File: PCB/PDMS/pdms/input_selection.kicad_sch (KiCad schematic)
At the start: 31 parts, among them U1 AQY221R4VY, U4 AQY221R4VY, U5 AQY221R4VY, U6 AQY221R4VY

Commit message: Clean-up of schematics
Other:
- note added: "Remember about pull down if safety future is used! R39..R42"
- note added: "Safety section (safety line handler)"
- note added: "TODO Rev 3.0: Add pull-down to all 16-channels input"
- note added: "https://www.mouser.pl/ProductDetail/Panasonic-Industrial-Devices/AQY221R4VY"
- note removed: "PlEASE CLEAN ME UP IF YOU HAVE MORE TIME!!!"
- note removed: "Remember about pull down if safety future is used!"
- note removed: "https://www.mouser.pl/ProductDetail/Panasonic-Industrial-Devices/AQY221R4VY?qs=St27ATL478uV4j9hHKsfjA%3D%3D"
- moved on the sheet: R1, R116, R117, R118, R119, R159, R160, R161, R162, R163, R164, R165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

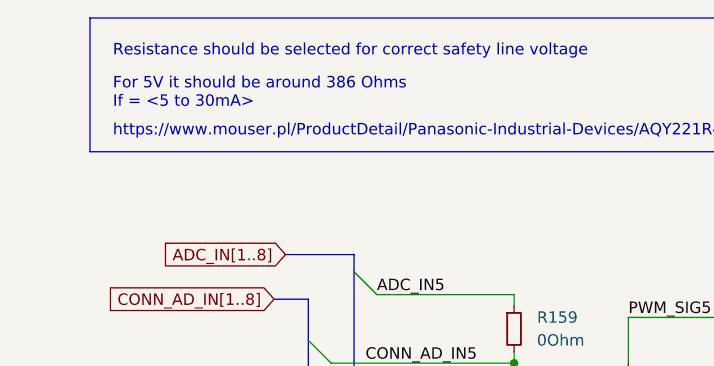
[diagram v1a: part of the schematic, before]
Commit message: Changes after board 4.1 first unit assembly
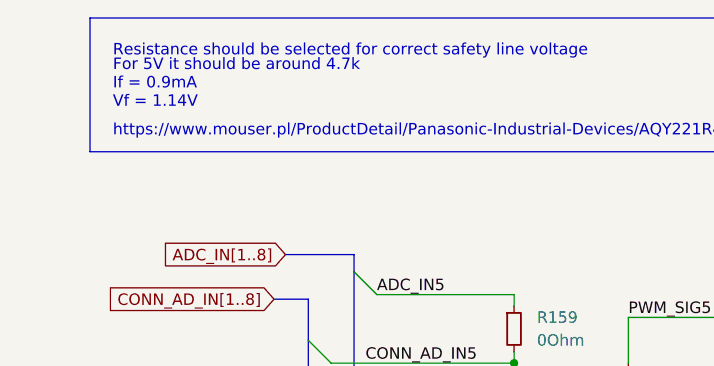
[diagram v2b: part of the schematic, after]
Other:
- note added: "For 5V it should be around 4.7k If = 0.9mA Vf = 1.14V"
- note removed: "For 5V it should be around 386 Ohms If = <5 to 30mA>"
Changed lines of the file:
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@@
     (data
       iVBORw0KGgoAAAANSUhEUgAABEQAAAI9CAIAAAC8GjpHAAAAA3NCSVQICAjb4U/gAAAACXBIWXMA
-      AA7DAAAOwwHHb6hkAAAgAElEQVR4nOy9ebhlRXnv/33fqjXs4czdp2lAECIgDqBB4xC9Md6f6DWo
+      AA50AAAOdAFrJLPWAAAgAElEQVR4nOy9ebhlRXnv/33fqjXs4czdp2lAECIgDqBB4xC9Md6f6DWo
       wXhFFMUhCXo1Go3DvcYBxSm5zpqoMUZ9xAGSnxpxiLNJjJo4YmKiIiJDAz2dYY9rqKr3/lF7r969
       zyCN9Ok+fep9zrPO2jW8n1q16ll7vfuteotEZM+ePfPz8yJCRM45Zq6OIgKAiJgZB8uquV6JP7fW
@@
     (effects (font (size 1.27 1.27)) (justify left bottom))
   )
-  (text "For 5V it should be around 386 Ohms\nIf = <5 to 30mA>"
+  (text "For 5V it should be around 4.7k\nIf = 0.9mA\nVf = 1.14V\n"
     (at 34.544 22.352 0)
     (effects (font (size 1.27 1.27)) (justify left bottom))

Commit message: Minor changes in overall schematics & MP4322 scheamtics
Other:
- note added: "Not applicable ->"
- note added: "X"
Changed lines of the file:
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@@
     (effects (font (size 2 2)) (justify left bottom))
+  )
+  (text "Not applicable ->" (at 114.935 136.525 0)
+    (effects (font (size 1.27 1.27)) (justify left bottom))
+  )
+  (text "Not applicable ->" (at 114.935 174.625 0)
+    (effects (font (size 1.27 1.27)) (justify left bottom))
   )
   (text "Safety section (safety line handler)" (at 99.568 277.876 0)
     (effects (font (size 2 2) italic) (justify left bottom))
   )
+  (text "X" (at 137.16 137.16 0)
+    (effects (font (size 3 3) (thickness 0.6) bold) (justify left bottom))
+  )
+  (text "X" (at 137.16 101.6 0)
+    (effects (font (size 3 3) (thickness 0.6) bold) (justify left bottom))
+  )
+  (text "Not applicable ->" (at 114.935 100.33 0)
+    (effects (font (size 1.27 1.27)) (justify left bottom))
+  )
   (text "Resistance should be selected for correct safety line voltage"
     (at 34.544 16.637 0)
@@
     (at 34.544 25.527 0)
     (effects (font (size 1.27 1.27)) (justify left bottom))
+  )
+  (text "X" (at 137.16 63.5 0)
+    (effects (font (size 3 3) (thickness 0.6) bold) (justify left bottom))
+  )
+  (text "Not applicable ->" (at 114.935 63.5 0)
+    (effects (font (size 1.27 1.27)) (justify left bottom))
+  )
+  (text "X" (at 137.16 175.26 0)
+    (effects (font (size 3 3) (thickness 0.6) bold) (justify left bottom))
   )
   (text "TODO Rev 3.0:\nAdd pull-down to all 16-channels input"
@@
   )
   (symbol (lib_id "Device:R_Small") (at 138.811 60.706 270) (unit 1)
-    (in_bom yes) (on_board yes) (fields_autoplaced)
-    (property "Reference" "R1" (id 0) (at 136.906 64.516 90)
-      (effects (font (size 1.27 1.27)) (justify left))
-    )
-    (property "Value" "0Ohm" (id 1) (at 136.271 62.611 90)
+    (in_bom yes) (on_board yes)
+    (property "Reference" "R1" (id 0) (at 137.16 66.04 90)
+      (effects (font (size 1.27 1.27)) (justify left))
+    )
+    (property "Value" "0Ohm" (id 1) (at 136.525 64.135 90)
       (effects (font (size 1.27 1.27)) (justify left))
     )
@@
   )
   (symbol (lib_id "Device:R_Small") (at 138.811 98.806 270) (unit 1)
-    (in_bom yes) (on_board yes) (fields_autoplaced)
-    (property "Reference" "R2" (id 0) (at 136.271 103.886 90)
-      (effects (font (size 1.27 1.27)) (justify left))
-    )
-    (property "Value" "0Ohm" (id 1) (at 136.271 101.346 90)
+    (in_bom yes) (on_board yes)
+    (property "Reference" "R2" (id 0) (at 136.525 104.775 90)
+      (effects (font (size 1.27 1.27)) (justify left))
+    )
+    (property "Value" "0Ohm" (id 1) (at 136.525 102.235 90)
       (effects (font (size 1.27 1.27)) (justify left))
     )
@@
   )
   (symbol (lib_id "Device:R_Small") (at 138.811 134.366 270) (unit 1)
-    (in_bom yes) (on_board yes) (fields_autoplaced)
-    (property "Reference" "R3" (id 0) (at 136.271 139.446 90)
-      (effects (font (size 1.27 1.27)) (justify left))
-    )
-    (property "Value" "0Ohm" (id 1) (at 136.271 136.906 90)
+    (in_bom yes) (on_board yes)
+    (property "Reference" "R3" (id 0) (at 136.525 140.335 90)
+      (effects (font (size 1.27 1.27)) (justify left))
+    )
+    (property "Value" "0Ohm" (id 1) (at 136.525 137.795 90)
       (effects (font (size 1.27 1.27)) (justify left))
     )
@@
   )
   (symbol (lib_id "Device:R_Small") (at 138.811 172.466 270) (unit 1)
-    (in_bom yes) (on_board yes) (fields_autoplaced)
-    (property "Reference" "R4" (id 0) (at 136.271 177.546 90)
-      (effects (font (size 1.27 1.27)) (justify left))
-    )
-    (property "Value" "0Ohm" (id 1) (at 136.271 175.006 90)
-      (effects (font (size 1.27 1.27)) (justify left))
-    )
+    (in_bom yes) (on_board yes)
+    (property "Reference" "R4" (id 0) (at 136.525 178.435 90)
+      (effects (font (size 1.27 1.27)) (justify left))
+    )
+    (property "Value" "0Ohm" (id 1) (at 136.525 175.895 90)
+      (effects (font (size 1.27 1.27)) (justify left))
+    )

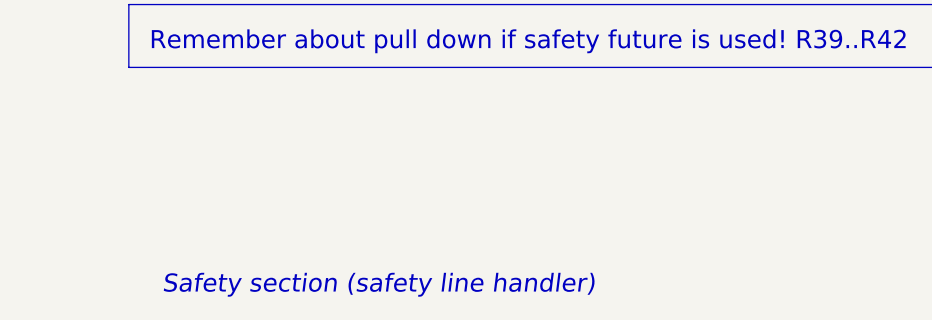
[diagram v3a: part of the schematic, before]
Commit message: WIP PCB folder structure and schematic clean-up
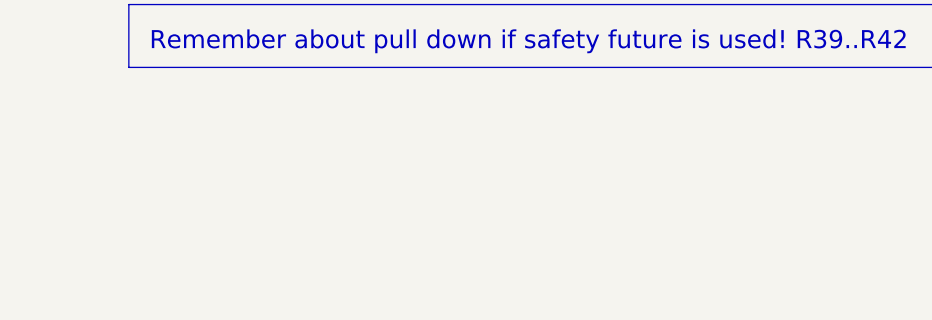
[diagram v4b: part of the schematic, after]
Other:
- note removed: "Safety section (safety line handler)"
- company: (none) -> PGRacing Team
- title: (none) -> Safety section (safety line handler)
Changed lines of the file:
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@@
 (kicad_sch (version 20211123) (generator eeschema)
   (paper "A4" portrait)
+  (title_block
+    (title "Safety section (safety line handler)")
+    (rev "V4.2")
+    (company "PGRacing Team")
+    (comment 1 "Karol Pergoł")
+  )
   (junction (at 135.001 169.926) (diameter 0) (color 0 0 0 0)
   )
@@
     (effects (font (size 1.27 1.27)) (justify left bottom))
   )
-  (text "Safety section (safety line handler)" (at 99.568 277.876 0)
-    (effects (font (size 2 2) italic) (justify left bottom))
-  )
   (text "X" (at 137.16 137.16 0)

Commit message: PDMS PCB input modification WIP - no supply
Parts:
- added D59, D60, D61, D62: TSD05, Diode_SMD:D_SOD-323, symbol Device:D_TVS
- R1, R160, R162, R164, R166, R2, R3, R4: now not fitted
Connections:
- net CONN_AD_IN5: now also D59.1 (A1)
- net CONN_AD_IN6: now also D60.1 (A1)
- net CONN_AD_IN7: now also D61.1 (A1)
- net CONN_AD_IN8: now also D62.1 (A1)
- net GND: now also D59.2 (A2), D60.2 (A2), D61.2 (A2), D62.2 (A2)
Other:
- note removed: "X"
- moved on the sheet: R39, R40, R41, R42

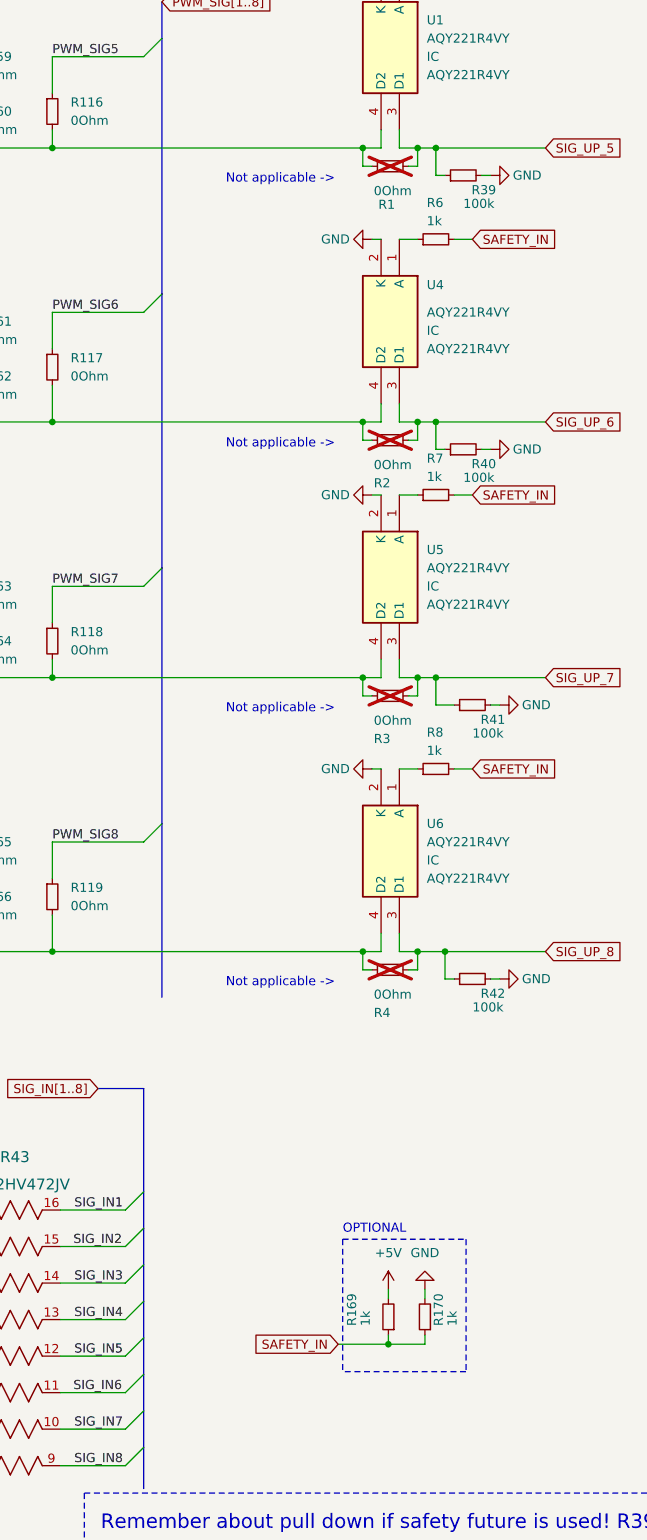
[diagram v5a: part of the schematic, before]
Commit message: PDMS PCB WIP modification mp4322 finished layput, cleared USB-C layout, moved OSC32 for better fit
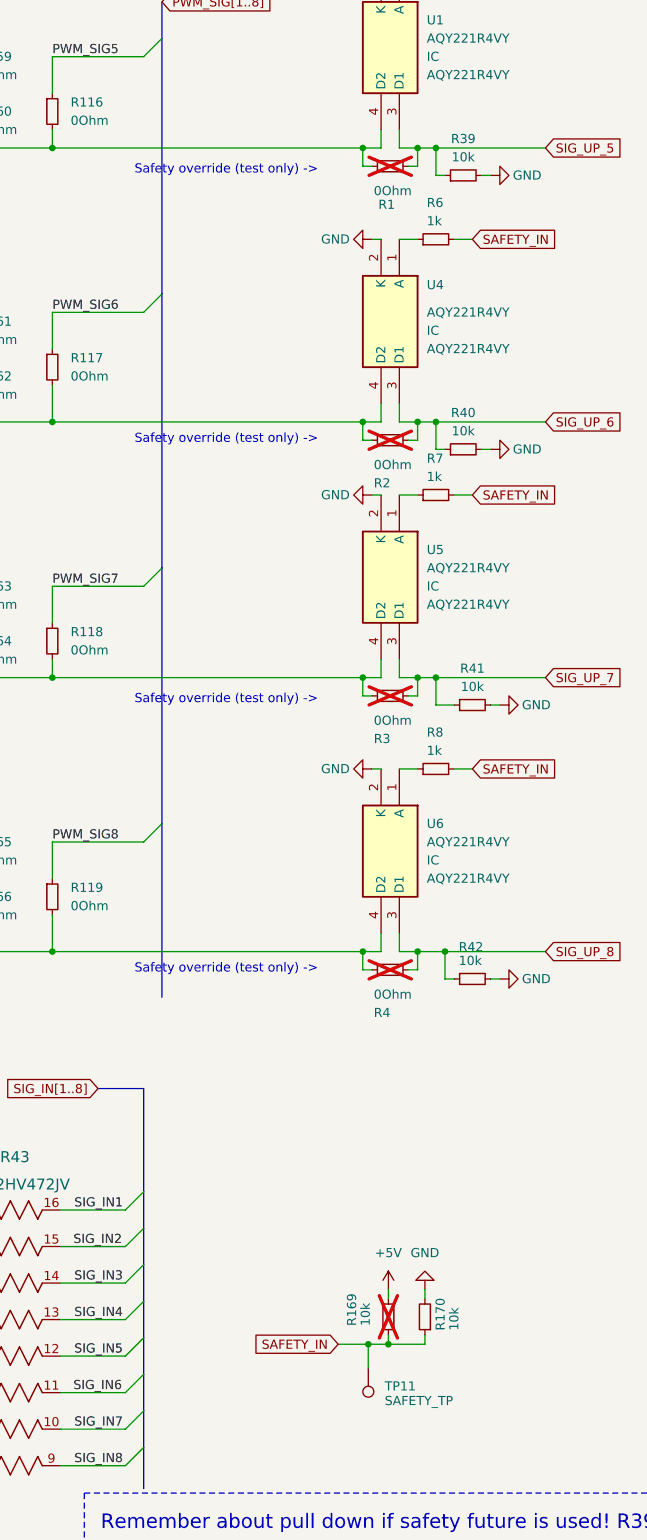
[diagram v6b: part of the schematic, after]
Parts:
- added TP11: SAFETY_TP, TestPoint:TestPoint_Pad_D2.0mm, symbol Connector:TestPoint
- R169: value 1k -> 10k; now not fitted
- R170: value 1k -> 10k
- R39, R40, R41, R42: value 100k -> 10k
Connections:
- net SAFETY_IN: now also TP11.1
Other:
- note added: "Safety override (test only) ->"
- note removed: "Not applicable ->"
- note removed: "OPTIONAL"
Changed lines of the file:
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@@
 	)
 	(junction
+		(at 135.382 224.79)
+		(diameter 0)
+		(color 0 0 0 0)
+	)
+	(junction
 		(at 134.62 132.08)
 		(diameter 0)
@@
 		)
 	)
-	(polyline
-		(pts
-			(xy 131.826 210.185) (xy 148.971 210.185)
-		)
-		(stroke
-			(width 0)
-			(type dash)
-		)
-	)
 	(wire
 		(pts
@@
 	(wire
 		(pts
+			(xy 135.382 224.79) (xy 135.382 228.092)
+		)
+		(stroke
+			(width 0)
+			(type default)
+		)
+	)
+	(wire
+		(pts
 			(xy 78.74 152.4) (xy 78.74 153.67)
 		)
@@
 		)
 	)
-	(polyline
-		(pts
-			(xy 148.971 210.185) (xy 148.971 228.6)
-		)
-		(stroke
-			(width 0)
-			(type dash)
-		)
-	)
 	(wire
 		(pts
@@
 		)
 	)
-	(polyline
-		(pts
-			(xy 131.826 210.185) (xy 131.826 228.6)
-		)
-		(stroke
-			(width 0)
-			(type dash)
-		)
-	)
 	(wire
 		(pts
@@
 		)
 	)
-	(polyline
-		(pts
-			(xy 148.971 228.6) (xy 131.826 228.6)
-		)
-		(stroke
-			(width 0)
-			(type dash)
-		)
-	)
 	(wire
 		(pts
@@
 	(wire
 		(pts
+			(xy 135.382 224.79) (xy 138.176 224.79)
+		)
+		(stroke
+			(width 0)
+			(type default)
+		)
+	)
+	(wire
+		(pts
 			(xy 140.97 134.62) (xy 142.24 134.62)
 		)
@@
 	(wire
 		(pts
-			(xy 131.191 224.79) (xy 138.176 224.79)
+			(xy 131.191 224.79) (xy 135.382 224.79)
 		)
 		(stroke
@@
 		)
 	)
-	(text "OPTIONAL"
-		(exclude_from_sim no)
-		(at 131.826 209.55 0)
-		(effects
-			(font
-				(size 1.27 1.27)
-			)
-			(justify left bottom)
-		)
-	)
 	(text "For 5V it should be around 4.7k\nIf = 0.9mA\nVf = 1.14V\n"
 		(exclude_from_sim no)
@@
 		)
 	)
-	(text "Not applicable ->"
+	(text "Safety override (test only) ->"
 		(exclude_from_sim no)
-		(at 115.57 137.16 0)
+		(at 102.87 135.89 0)
 		(effects
 			(font
@@
 		)
 	)
-	(text "Not applicable ->"
+	(text "Safety override (test only) ->"
 		(exclude_from_sim no)
-		(at 115.57 175.26 0)
+		(at 102.87 173.355 0)
 		(effects
 			(font
@@
 		)
 	)
-	(text "Not applicable ->"
+	(text "Resistance should be selected for correct safety line voltage"
 		(exclude_from_sim no)
-		(at 115.57 100.33 0)
+		(at 34.544 16.637 0)
 		(effects
 			(font
@@
 		)
 	)
-	(text "Resistance should be selected for correct safety line voltage"
+	(text "https://www.mouser.pl/ProductDetail/Panasonic-Industrial-Devices/AQY221R4VY"
 		(exclude_from_sim no)
-		(at 34.544 16.637 0)
+		(at 34.29 25.4 0)
 		(effects
 			(font
@@
 		)
 	)
-	(text "https://www.mouser.pl/ProductDetail/Panasonic-Industrial-Devices/AQY221R4VY"
+	(text "Safety override (test only) ->"
 		(exclude_from_sim no)
-		(at 34.29 25.4 0)
+		(at 102.87 62.23 0)
 		(effects
 			(font
@@
 		)
 	)
-	(text "Not applicable ->"
+	(text "Safety override (test only) ->"
 		(exclude_from_sim no)
-		(at 115.57 63.5 0)
+		(at 102.87 99.695 0)
 		(effects
 			(font
@@
 		(dnp no)
 		(property "Reference" "R170"
-			(at 145.161 222.25 90)
+			(at 145.415 222.885 90)
 			(effects
 				(font
@@
 			)
 		)
-		(property "Value" "1k"
-			(at 147.066 222.25 90)
+		(property "Value" "10k"
+			(at 147.32 222.885 90)
 			(effects
 				(font
@@
 		(fields_autoplaced yes)
 		(property "Reference" "R40"
-			(at 149.733 102.362 90)
+			(at 148.59 95.25 90)
 			(effects
 				(font
 					(size 1.27 1.27)
 				)
-				(justify right)
 			)
 		)
-		(property "Value" "100k"
-			(at 148.59 104.267 90)
+		(property "Value" "10k"
+			(at 148.59 97.79 90)
 			(effects
 				(font
 					(size 1.27 1.27)
 				)
-				(justify right)
 			)
 		)
@@
 		(on_board yes)
 		(dnp no)
-		(fields_autoplaced yes)
 		(property "Reference" "R41"
-			(at 151.003 137.922 90)
+			(at 149.86 130.81 90)
 			(effects
 				(font
 					(size 1.27 1.27)
 				)
-				(justify right)
 			)
 		)
-		(property "Value" "100k"
-			(at 149.86 139.827 90)
+		(property "Value" "10k"
+			(at 149.86 133.35 90)
 			(effects
 				(font
 					(size 1.27 1.27)
 				)
-				(justify right)
 			)
 		)
@@
 	)
 	(symbol
+		(lib_id "Connector:TestPoint")
+		(at 135.382 228.092 180)
+		(unit 1)
+		(exclude_from_sim no)
+		(in_bom yes)
+		(on_board yes)
+		(dnp no)
+		(property "Reference" "TP11"
+			(at 137.668 230.632 0)
+			(effects
+				(font
+					(size 1.27 1.27)
+				)
+				(justify right)
+			)
+		)
+		(property "Value" "SAFETY_TP"
+			(at 137.668 232.664 0)
+			(effects
+				(font
+					(size 1.27 1.27)
+				)
+				(justify right)
+			)
+		)
+		(property "Footprint" "TestPoint:TestPoint_Pad_D2.0mm"
+			(at 130.302 228.092 0)
+			(effects
+				(font
+					(size 1.27 1.27)
+				)
+				(hide yes)
+			)
+		)
+		(property "Datasheet" "~"
+			(at 130.302 228.092 0)
+			(effects
+				(font
+					(size 1.27 1.27)
+				)
+				(hide yes)
+			)
+		)
+		(property "Description" "test point"
+			(at 135.382 228.092 0)
+			(effects
+				(font
+					(size 1.27 1.27)
+				)
+				(hide yes)
+			)
+		)
+		(pin "1"
+		)
+		(instances
+			(project "pdms"
+				(path "/d3407657-4284-42d4-8012-68a1da9eff64/5e0d1f91-4fae-411e-a2b8-95f4b4fcadc5"
+					(reference "TP11")
+					(unit 1)
+				)
+			)
+		)
+	)
+	(symbol
 		(lib_id "Device:R_Small")
 		(at 149.86 173.99 90)
@@
 		(on_board yes)
 		(dnp no)
-		(fields_autoplaced yes)
 		(property "Reference" "R42"
-			(at 151.003 176.022 90)
+			(at 147.955 169.545 90)
 			(effects
 				(font
@@
 			)
 		)
-		(property "Value" "100k"
-			(at 149.86 177.927 90)
+		(property "Value" "10k"
+			(at 147.955 171.45 90)
 			(effects
 				(font
@@
 		(fields_autoplaced yes)
 		(property "Reference" "R39"
-			(at 149.733 64.262 90)
+			(at 148.59 57.15 90)
 			(effects
 				(font
 					(size 1.27 1.27)
 				)
-				(justify right)
 			)
 		)
-		(property "Value" "100k"
-			(at 148.59 66.167 90)
+		(property "Value" "10k"
+			(at 148.59 59.69 90)
 			(effects
 				(font
 					(size 1.27 1.27)
 				)
-				(justify right)
 			)
 		)
@@
 		(in_bom yes)
 		(on_board yes)
-		(dnp no)
+		(dnp yes)
 		(property "Reference" "R169"
 			(at 133.096 222.25 90)
@@
 			)
 		)
-		(property "Value" "1k"
+		(property "Value" "10k"
 			(at 135.001 222.25 90)
 			(effects
